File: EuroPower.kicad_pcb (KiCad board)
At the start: 2 copper layers, 182.9 x 30.5 mm, 27 parts, among them J1 Screw_Terminal_01x03, J10 Screw_Terminal_01x03, J2 Conn_02x05_Odd_Even, J3 Conn_02x05_Odd_Even, J4 Conn_02x05_Odd_Even, J5 Conn_02x05_Odd_Even, J6 Conn_02x05_Odd_Even, J7 Conn_02x05_Odd_Even, J8 Conn_02x05_Odd_Even, J9 Conn_02x05_Odd_Even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

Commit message: Ground pours.
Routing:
- net +12V: track 217.6 -> 618.9 mm
- added copper zone on B.Cu, net GND
- added copper zone on F.Cu, net GND
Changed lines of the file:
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@@
   (general
     (links 105)
-    (no_connects 105)
-    (area 33.225714 88.824999 220.774286 119.455001)
+    (no_connects 0)
+    (area 9.930001 76.04 238.99 132.240001)
     (thickness 1.6)
     (drawings 9)
-    (tracks 93)
+    (tracks 114)
     (zones 0)
     (modules 27)
@@
   (segment (start 167.64 116.402144) (end 167.64 114.3) (width 2) (layer F.Cu) (net 2))
   (segment (start 187.96 115.53) (end 177.8 115.53) (width 2) (layer F.Cu) (net 2))
-  (segment (start 111.76 114.3) (end 115.57 114.3) (width 0.25) (layer F.Cu) (net 3))
-  (segment (start 142.24 114.3) (end 138.43 114.3) (width 0.25) (layer F.Cu) (net 4))
+  (segment (start 111.76 114.3) (end 115.57 114.3) (width 0.5) (layer F.Cu) (net 3))
+  (segment (start 138.43 114.3) (end 142.24 114.3) (width 0.5) (layer F.Cu) (net 4))
+  (segment (start 54.61 96.52) (end 197.344002 96.52) (width 2) (layer F.Cu) (net 6))
+  (segment (start 197.344002 96.52) (end 199.39 96.52) (width 2) (layer F.Cu) (net 6))
+  (segment (start 196.85 96.52) (end 199.39 96.52) (width 2) (layer F.Cu) (net 6))
+  (segment (start 57.15 96.52) (end 197.344002 96.52) (width 2) (layer B.Cu) (net 6))
+  (segment (start 197.344002 96.52) (end 199.39 96.52) (width 2) (layer B.Cu) (net 6))
+  (segment (start 54.61 96.52) (end 57.15 96.52) (width 2) (layer B.Cu) (net 6))
+  (segment (start 138.43 96.52) (end 156.21 96.52) (width 2) (layer F.Cu) (net 6))
+  (segment (start 118.11 96.52) (end 135.89 96.52) (width 2) (layer F.Cu) (net 6))
+  (segment (start 93.98 96.52) (end 95.25 96.52) (width 2) (layer F.Cu) (net 6))
+  (segment (start 76.2 96.52) (end 93.98 96.52) (width 2) (layer F.Cu) (net 6))
+  (segment (start 93.98 96.52) (end 97.79 96.52) (width 2) (layer F.Cu) (net 6))
+  (segment (start 76.2 96.52) (end 77.47 96.52) (width 2) (layer F.Cu) (net 6))
+  (segment (start 73.66 96.52) (end 76.2 96.52) (width 2) (layer F.Cu) (net 6))
+  (segment (start 73.66 96.52) (end 74.93 96.52) (width 2) (layer F.Cu) (net 6))
+  (segment (start 57.15 96.52) (end 73.66 96.52) (width 2) (layer F.Cu) (net 6))
+  (segment (start 177.8 96.52) (end 179.07 96.52) (width 2) (layer B.Cu) (net 6))
+  (segment (start 175.26 96.52) (end 177.8 96.52) (width 2) (layer B.Cu) (net 6))
+  (segment (start 177.8 96.52) (end 196.85 96.52) (width 2) (layer B.Cu) (net 6))
+  (segment (start 158.75 96.52) (end 176.53 96.52) (width 2) (layer B.Cu) (net 6))
+  (segment (start 156.21 96.52) (end 158.75 96.52) (width 2) (layer B.Cu) (net 6))
+  (segment (start 134.62 96.52) (end 135.89 96.52) (width 2) (layer B.Cu) (net 6))
+  (segment (start 118.11 96.52) (end 134.62 96.52) (width 2) (layer B.Cu) (net 6))
+  (segment (start 134.62 96.52) (end 138.43 96.52) (width 2) (layer B.Cu) (net 6))
+  (segment (start 114.3 96.52) (end 115.57 96.52) (width 2) (layer B.Cu) (net 6))
+  (segment (start 96.52 96.52) (end 114.3 96.52) (width 2) (layer B.Cu) (net 6))
+  (segment (start 114.3 96.52) (end 118.11 96.52) (width 2) (layer B.Cu) (net 6))
+  (segment (start 96.52 96.52) (end 97.79 96.52) (width 2) (layer B.Cu) (net 6))
+  (segment (start 95.25 96.52) (end 96.52 96.52) (width 2) (layer B.Cu) (net 6))
+  (segment (start 77.47 96.52) (end 95.25 96.52) (width 2) (layer B.Cu) (net 6))
+  (segment (start 77.47 96.52) (end 74.93 96.52) (width 2) (layer B.Cu) (net 6))
   (segment (start 54.61 96.52) (end 52.099538 96.52) (width 2) (layer F.Cu) (net 6))
   (segment (start 52.099538 96.52) (end 50.207413 98.412125) (width 2) (layer F.Cu) (net 6))
@@
   (segment (start 94.570161 111.080161) (end 95.720001 112.230001) (width 2) (layer F.Cu) (net 6))
   (segment (start 95.720001 112.230001) (end 96.52 113.03) (width 2) (layer F.Cu) (net 6))
-  (segment (start 77.47 96.52) (end 87.63 96.52) (width 2) (layer F.Cu) (net 6))
-  (segment (start 87.63 96.52) (end 95.25 96.52) (width 2) (layer F.Cu) (net 6))
-  (segment (start 118.11 96.52) (end 135.89 96.52) (width 2) (layer F.Cu) (net 6))
-  (segment (start 196.85 96.52) (end 199.39 96.52) (width 2) (layer F.Cu) (net 6))
   (segment (start 179.07 96.52) (end 196.85 96.52) (width 2) (layer F.Cu) (net 6))
   (segment (start 176.53 96.52) (end 179.07 96.52) (width 2) (layer F.Cu) (net 6))
@@
   (segment (start 157.48 96.52) (end 175.26 96.52) (width 2) (layer F.Cu) (net 6))
   (segment (start 175.26 96.52) (end 176.53 96.52) (width 2) (layer F.Cu) (net 6))
-  (segment (start 138.43 96.52) (end 156.21 96.52) (width 2) (layer F.Cu) (net 6))
   (segment (start 135.89 96.52) (end 138.43 96.52) (width 2) (layer F.Cu) (net 6))
   (segment (start 115.57 96.52) (end 118.11 96.52) (width 2) (layer F.Cu) (net 6))
   (segment (start 97.79 96.52) (end 115.57 96.52) (width 2) (layer F.Cu) (net 6))
-  (segment (start 95.25 96.52) (end 97.79 96.52) (width 2) (layer F.Cu) (net 6))
-  (segment (start 74.93 96.52) (end 77.47 96.52) (width 2) (layer F.Cu) (net 6))
-  (segment (start 57.15 96.52) (end 74.93 96.52) (width 2) (layer F.Cu) (net 6))
-  (segment (start 54.61 96.52) (end 57.15 96.52) (width 2) (layer F.Cu) (net 6))
   (segment (start 77.47 106.68) (end 95.25 106.68) (width 2) (layer F.Cu) (net 7))
   (segment (start 157.48 110.49) (end 158.75 109.22) (width 2) (layer F.Cu) (net 7))
@@
   (segment (start 57.15 106.68) (end 74.93 106.68) (width 2) (layer F.Cu) (net 7))
   (segment (start 54.61 106.68) (end 57.15 106.68) (width 2) (layer F.Cu) (net 7))
+  (zone (net 5) (net_name GND) (layer B.Cu) (hatch edge 0.508)
+    (connect_pads (clearance 0.508))
+    (min_thickness 0.254)
+    (fill yes (arc_segments 16) (thermal_gap 0.508) (thermal_bridge_width 0.508))
+    (polygon
+      (pts
+        (xy 35.56 88.9) (xy 218.44 88.9) (xy 218.44 119.38) (xy 35.56 119.38)
+      )
+    )
+  )
+  (zone (net 5) (net_name GND) (layer F.Cu) (hatch edge 0.508)
+    (connect_pads (clearance 0.508))
+    (min_thickness 0.254)
+    (fill yes (arc_segments 16) (thermal_gap 0.508) (thermal_bridge_width 0.508))
+    (polygon
+      (pts
+        (xy 218.44 88.9) (xy 218.44 119.38) (xy 35.56 119.38) (xy 35.56 88.9)
+      )
+    )
+  )
 )

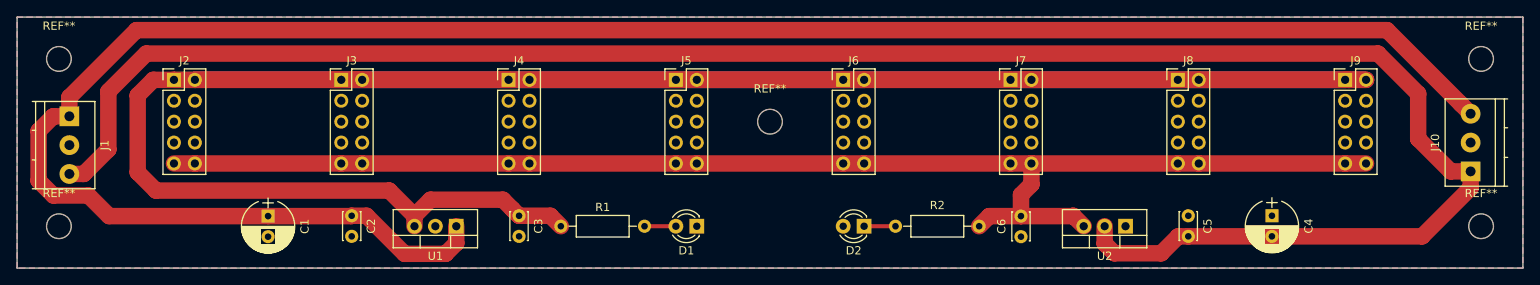
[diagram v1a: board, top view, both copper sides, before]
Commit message: Silkscreen layout.
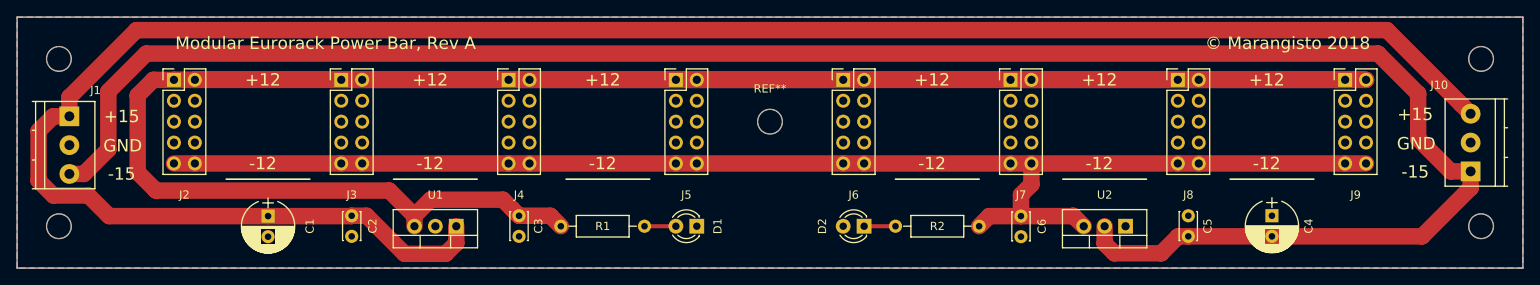
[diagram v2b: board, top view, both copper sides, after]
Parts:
- renumbered REF** to ?
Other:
- board text added: "+12"
- board text added: "+15"
- board text added: "-12"
- board text added: "-15"
- board text added: "GND"
- board text added: "Modular Eurorack Power Bar, Rev A"
- board text added: "© Marangisto 2018"
